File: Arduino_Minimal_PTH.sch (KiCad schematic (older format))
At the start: 21 parts, among them IC1 ATMEGA328P-PU, P1 I/O lo, P2 FTDI Basic, P3 A4 A5, P4 I/O hi, SW1 Reset, U1 L4931CZ50-AP, X1 CSTLS16M0X53-B0

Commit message: Placed.
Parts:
- removed C1: 10u, mfk-CRP_5.0_2.0_0.5, symbol CP1
- removed C3: 100n, mfk-C_4.0_2.5_2.5_0.5, symbol C
- removed D1, D2: LED, LED-3MM, symbol LED
- removed R1: 10K, mfk-R_0.25W_RN55_vert, symbol R
- removed R3: 330, mfk-R_0.25W_RN55_vert, symbol R
- removed R4, R5: opt, mfk-R_0.25W_RN55_vert, symbol R
- removed U1: L4931CZ50-AP, mfk-TO-92_f321, symbol L4931CZ50-AP
- C2: footprint mfk-CRP_5.0_2.0_0.5 -> mfk-CRP_4.0_2.5_0.5
- SW1: footprint mfk-SW_PUSH_6MM -> mfk-SW_PUSH_6x3.5mm
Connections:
- net RAW: no longer names the net of P4.1 (P1)
- no-connect marks 0 -> 1
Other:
- note added: "Apem MJTP1243 \nor MJTP1250"
- note added: "Removed:\nC1\nU1\nD1\nR1\nR3\nD2\nC3\nR4\nR5"
- note removed: "20V max input"
- note removed: "6mm N.O. tactile\n(e.g. TE 1977120-6,\nC&K PTS645SL43 LFS)"
- note removed: "For low power application,\ndo not populate U1, D1, R1."
- note removed: "Green"
- note removed: "Optional pullups for I2C"
- note removed: "Red"
- moved on the sheet: C2

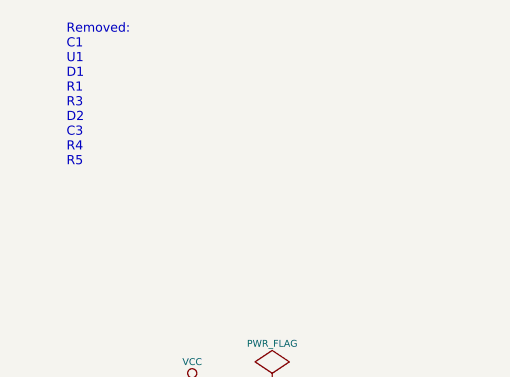
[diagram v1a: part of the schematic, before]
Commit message: Renamed doc -> docs.
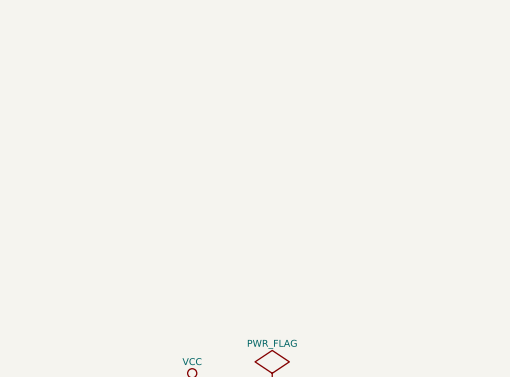
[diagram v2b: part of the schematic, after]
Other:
- note removed: "Removed:\nC1\nU1\nD1\nR1\nR3\nD2\nC3\nR4\nR5"
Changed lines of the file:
@@
 Sheet 1 1
 Title "Minimal Arduino using through-hole parts"
-Date "26 mar 2015"
+Date "27 mar 2015"
 Rev ""
 Comp "Mithat Konar (https://github.com/mithat/Arduino_Minimal_PTH)"
@@
 63 98 05 E1 6B C4 72 91 8E EA 95 27 8C 4B 0B 6B 30 6B 95 2D 08 DF 47 79 14 D8 40 20 A9 90 96 2D
 E1 E7 3D C6 74 F3 E0 6E B9 00 E4 0E CC EC 2A 00 9E 03 F9 2E 43 53 93 3B E7 B1 3D FE 0F E4 2C B5
-B8 3A B8 3B 5D 00 00 00 00 49 45 4E 44 AE 42 60 82 43 $EndBitmap
+B8 3A B8 3B 5D 00 00 00 00 49 45 4E 44 AE 42 60 82 33 $EndBitmap
 EndData
 $EndBitmap
@@
 $EndComp
 NoConn ~ 3000 5500
-Text Notes 950  1050 0    40   ~ 0
-Removed:\nC1\nU1\nD1\nR1\nR3\nD2\nC3\nR4\nR5
 Wire Wire Line
 	1850 2150 1850 2000
